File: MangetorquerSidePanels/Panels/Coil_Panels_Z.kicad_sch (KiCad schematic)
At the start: 7 parts, among them J1 Through_Hole_1, J2 MOLEX_2053380006

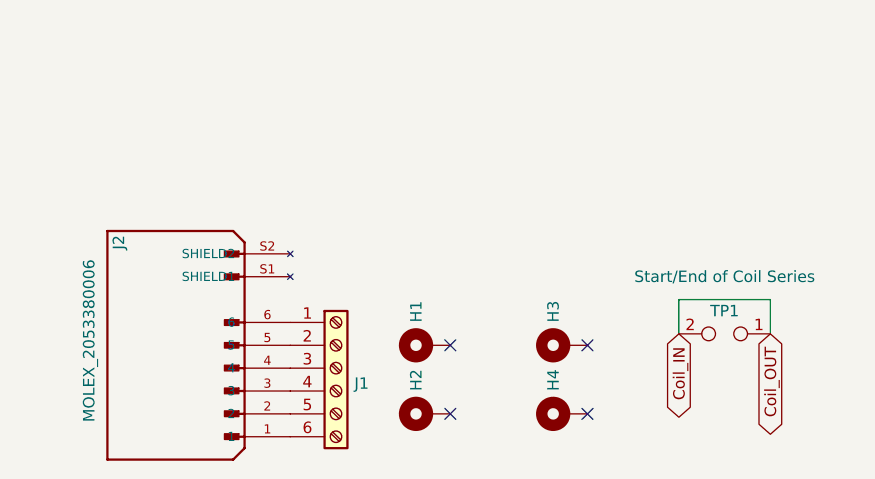
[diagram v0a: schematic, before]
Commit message: Final flight side panels w/ magnetorquers finished, note final board thickness of 0.031'' and updated copper weight of 0.5oz for internal layers
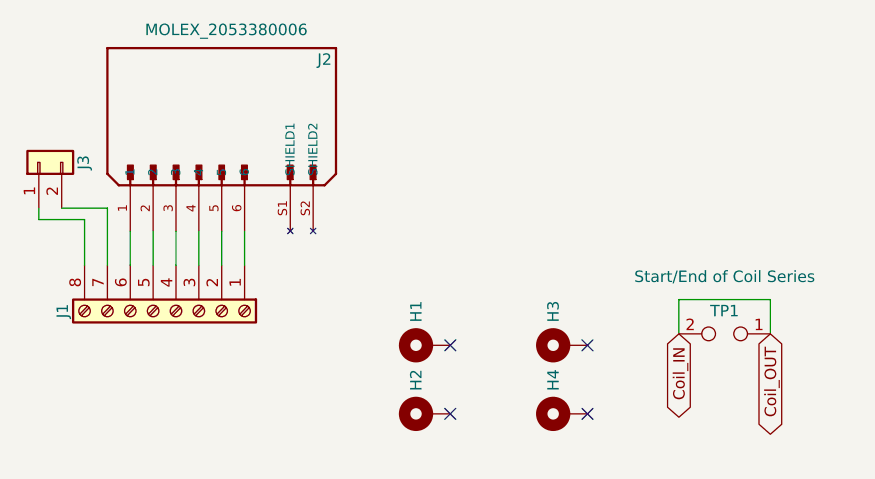
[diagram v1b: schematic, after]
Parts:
- removed J1: Through_Hole_1, Connector_PinHeader_2.54mm:PinHeader_1x06_P2.54mm_Vertical, symbol Connector:Screw_Terminal_01x06
- added J1: Screw_Terminal_01x08, Connector_PinHeader_2.54mm:PinHeader_1x08_P2.54mm_Vertical, symbol Connector:Screw_Terminal_01x08
- added J3: Conn_01x02, panels:2053380002, symbol Connector_Generic:Conn_01x02
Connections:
- net at J2.1: now also J1.6 (Pin_6)
- net at J2.2: now also J1.5 (Pin_5)
- net at J2.3: now also J1.4 (Pin_4)
- net at J2.4: now also J1.3 (Pin_3)
- net at J2.5: now also J1.2 (Pin_2)
- net at J2.6: now also J1.1 (Pin_1)
- new net: J1.7 (Pin_7), J3.2 (Pin_2)
- new net: J1.8 (Pin_8), J3.1 (Pin_1)
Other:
- moved on the sheet: J2
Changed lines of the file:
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@@
+    (stroke (width 0) (type default) (color 0 0 0 0))
+  )
+  (wire (pts (xy 104.14 82.55) (xy 104.14 86.36))
+    (stroke (width 0) (type default) (color 0 0 0 0))
+  )
+  (wire (pts (xy 91.44 81.28) (xy 86.36 81.28))
+    (stroke (width 0) (type default) (color 0 0 0 0))
+  )
+  (wire (pts (xy 96.52 82.55) (xy 96.52 86.36))
     (stroke (width 0) (type default) (color 0 0 0 0))
   )
@@
     (stroke (width 0) (type default) (color 0 0 0 0))
   )
+  (wire (pts (xy 93.98 86.36) (xy 93.98 80.01))
+    (stroke (width 0) (type default) (color 0 0 0 0))
+  )
+  (wire (pts (xy 91.44 86.36) (xy 91.44 81.28))
+    (stroke (width 0) (type default) (color 0 0 0 0))
+  )
   (wire (pts (xy 157.48 90.17) (xy 167.64 90.17))
+    (stroke (width 0) (type default) (color 0 0 0 0))
+  )
+  (wire (pts (xy 86.36 81.28) (xy 86.36 80.01))
+    (stroke (width 0) (type default) (color 0 0 0 0))
+  )
+  (wire (pts (xy 88.9 80.01) (xy 93.98 80.01))
+    (stroke (width 0) (type default) (color 0 0 0 0))
+  )
+  (wire (pts (xy 106.68 82.55) (xy 106.68 86.36))
+    (stroke (width 0) (type default) (color 0 0 0 0))
+  )
+  (wire (pts (xy 101.6 82.55) (xy 101.6 86.36))
+    (stroke (width 0) (type default) (color 0 0 0 0))
+  )
+  (wire (pts (xy 99.06 82.55) (xy 99.06 86.36))
+    (stroke (width 0) (type default) (color 0 0 0 0))
+  )
+  (wire (pts (xy 109.22 82.55) (xy 109.22 86.36))
     (stroke (width 0) (type default) (color 0 0 0 0))
   )
@@
     (pin "2")
   )
-  (symbol (lib_id "solar-panel-side-X-plus-rescue:2053380006-sapling") (at 101.6 95.25 180) (unit 1)
-    (in_bom yes) (on_board yes)
-    (property "Reference" "J2" (id 0) (at 95.25 83.82 90))
-    (property "Value" "MOLEX_2053380006" (id 1) (at 91.948 94.742 90))
-    (property "Footprint" "panels:MOLEX_2053380006" (id 2) (at 101.6 95.25 0)
-      (effects (font (size 1.27 1.27)) hide)
-    )
-    (property "Datasheet" "https://www.molex.com/webdocs/datasheets/pdf/en-us/2053380006_PCB_HEADERS.pdf" (id 3) (at 101.6 95.25 0)
+  (symbol (lib_id "solar-panel-side-X-plus-rescue:2053380006-sapling") (at 106.68 69.85 90) (unit 1)
+    (in_bom yes) (on_board yes)
+    (property "Reference" "J2" (id 0) (at 118.11 63.5 90))
+    (property "Value" "MOLEX_2053380006" (id 1) (at 107.188 60.198 90))
+    (property "Footprint" "panels:MOLEX_2053380006" (id 2) (at 106.68 69.85 0)
+      (effects (font (size 1.27 1.27)) hide)
+    )
+    (property "Datasheet" "https://www.molex.com/webdocs/datasheets/pdf/en-us/2053380006_PCB_HEADERS.pdf" (id 3) (at 106.68 69.85 0)
       (effects (font (size 1.27 1.27)) hide)
     )
@@
     (pin "1")
   )
-  (symbol (lib_id "Connector:Screw_Terminal_01x06") (at 119.38 97.79 0) (unit 1)
+  (symbol (lib_id "Connector:Screw_Terminal_01x08") (at 101.6 91.44 270) (unit 1)
     (in_bom yes) (on_board yes) (fields_autoplaced)
-    (property "Reference" "J1" (id 0) (at 121.412 99.4938 0)
-      (effects (font (size 1.27 1.27)) (justify left))
-    )
-    (property "Value" "Through_Hole_1" (id 1) (at 125.2173 99.06 90)
-      (effects (font (size 1.27 1.27)) hide)
-    )
-    (property "Footprint" "Connector_PinHeader_2.54mm:PinHeader_1x06_P2.54mm_Vertical" (id 2) (at 119.38 97.79 0)
-      (effects (font (size 1.27 1.27)) hide)
-    )
-    (property "Datasheet" "~" (id 3) (at 119.38 97.79 0)
+    (property "Reference" "J1" (id 0) (at 89.0072 91.44 0))
+    (property "Value" "Screw_Terminal_01x08" (id 1) (at 98.6278 93.472 0)
+      (effects (font (size 1.27 1.27)) (justify left) hide)
+    )
+    (property "Footprint" "Connector_PinHeader_2.54mm:PinHeader_1x08_P2.54mm_Vertical" (id 2) (at 101.6 91.44 0)
+      (effects (font (size 1.27 1.27)) hide)
+    )
+    (property "Datasheet" "~" (id 3) (at 101.6 91.44 0)
       (effects (font (size 1.27 1.27)) hide)
     )
@@
     (pin "5")
     (pin "6")
+    (pin "7")
+    (pin "8")
+  )
+  (symbol (lib_id "Connector_Generic:Conn_01x02") (at 86.36 74.93 90) (unit 1)
+    (in_bom yes) (on_board yes) (fields_autoplaced)
+    (property "Reference" "J3" (id 0) (at 91.3328 74.93 0))
+    (property "Value" "Conn_01x02" (id 1) (at 91.3329 74.93 0)
+      (effects (font (size 1.27 1.27)) hide)
+    )
+    (property "Footprint" "panels:2053380002" (id 2) (at 86.36 74.93 0)
+      (effects (font (size 1.27 1.27)) hide)
+    )
+    (property "Datasheet" "~" (id 3) (at 86.36 74.93 0)
+      (effects (font (size 1.27 1.27)) hide)
+    )
+    (pin "1")
+    (pin "2")
   )
   (symbol (lib_id "Mechanical:MountingHole_Pad") (at 129.54 95.25 90) (unit 1)
@@
       (reference "H4") (unit 1) (value "~") (footprint "MountingHole:MountingHole_2.2mm_M2_DIN965_Pad_TopBottom")
     )
-    (path "/f354fac1-2138-41aa-b2af-c8cec7e009ae"
-      (reference "J1") (unit 1) (value "Through_Hole_1") (footprint "Connector_PinHeader_2.54mm:PinHeader_1x06_P2.54mm_Vertical")
+    (path "/cbb823db-aa27-4676-b554-52540ee4385b"
+      (reference "J1") (unit 1) (value "Screw_Terminal_01x08") (footprint "Connector_PinHeader_2.54mm:PinHeader_1x08_P2.54mm_Vertical")
     )
     (path "/7d363d4c-06ea-472e-bda1-3a6cd68a7642"
       (reference "J2") (unit 1) (value "MOLEX_2053380006") (footprint "panels:MOLEX_2053380006")
     )
+    (path "/d92e591b-fd8e-4746-a2c1-e51412792340"
+      (reference "J3") (unit 1) (value "Conn_01x02") (footprint "panels:2053380002")
+    )
     (path "/5baee474-40c4-4414-ac3a-a583b8c40a2f"
